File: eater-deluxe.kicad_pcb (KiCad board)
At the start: 2 copper layers, 214.2 x 149.5 mm, 39 parts, among them J1 PJ-202A, J2 DE9_Socket, SW1 RESET, U1 6502, U2 W65C22NxP, U3 W65C51NxP, U4 28C256, U5 HM62256BLP, U6 CD74HC00E, U7 MAX232, U8 LCD Module Connector, X1 MXO45-3C-1M000000, Y1 1.8432MHz

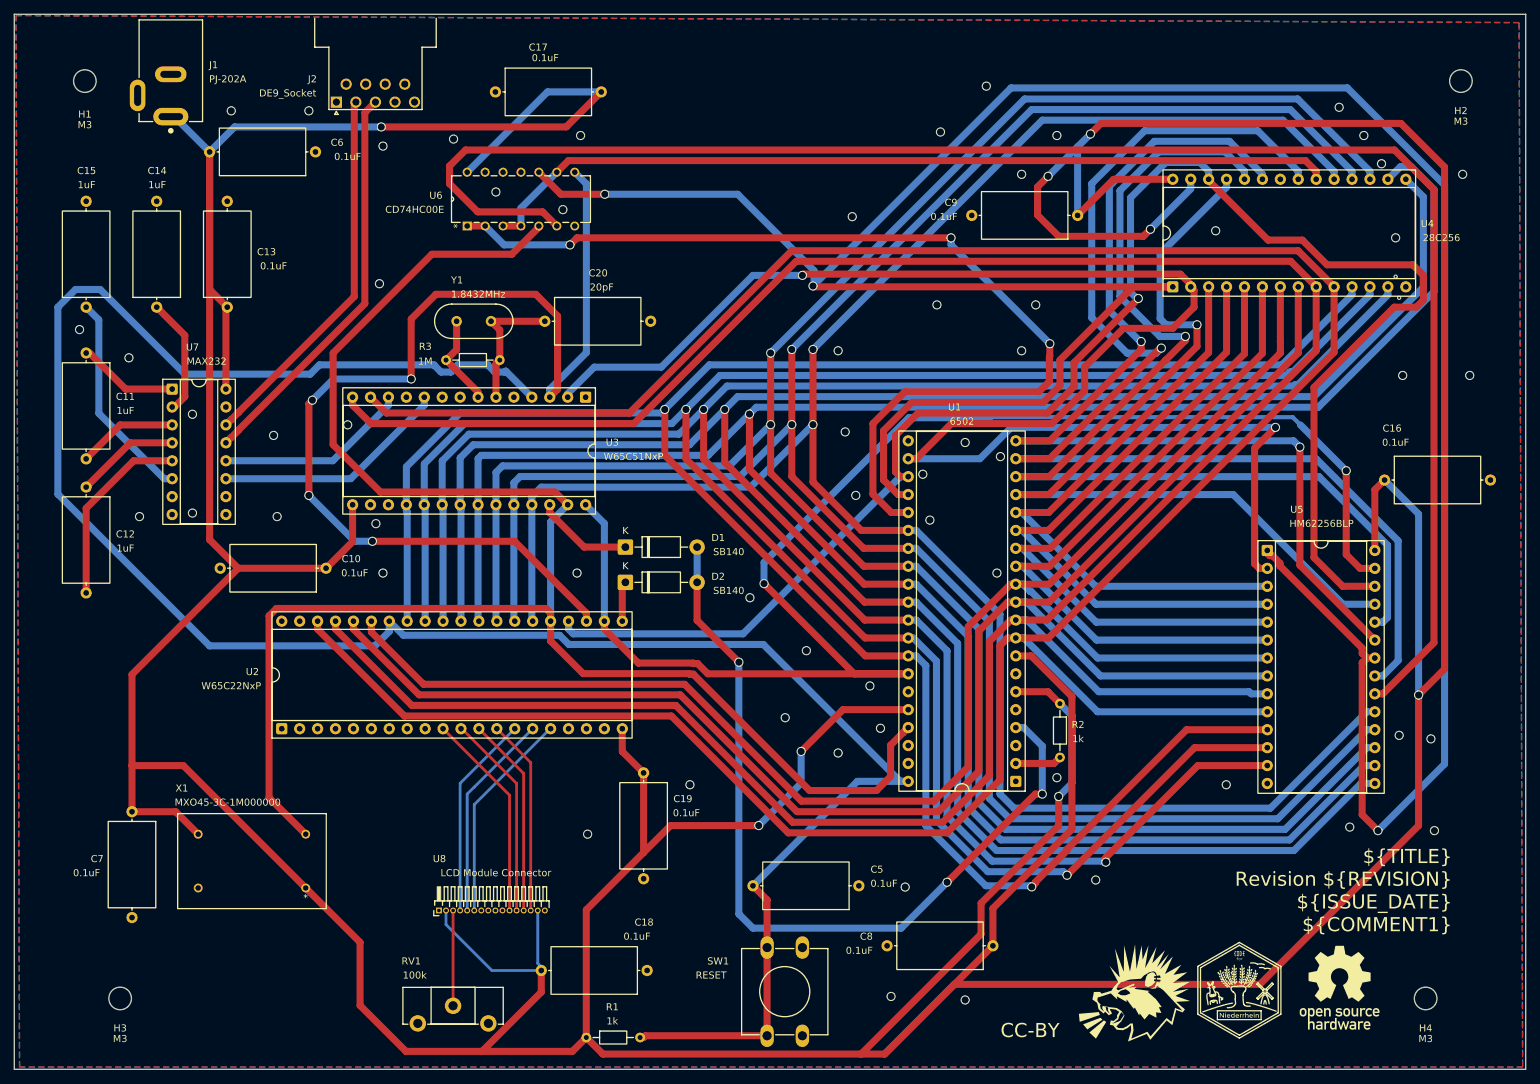
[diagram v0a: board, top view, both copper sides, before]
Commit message: Correct X1 pinout, fix LCD Pins, add pullup resistors for interrupt lines
Signed-off-by: Lucy Mielke <user@domain.tld>
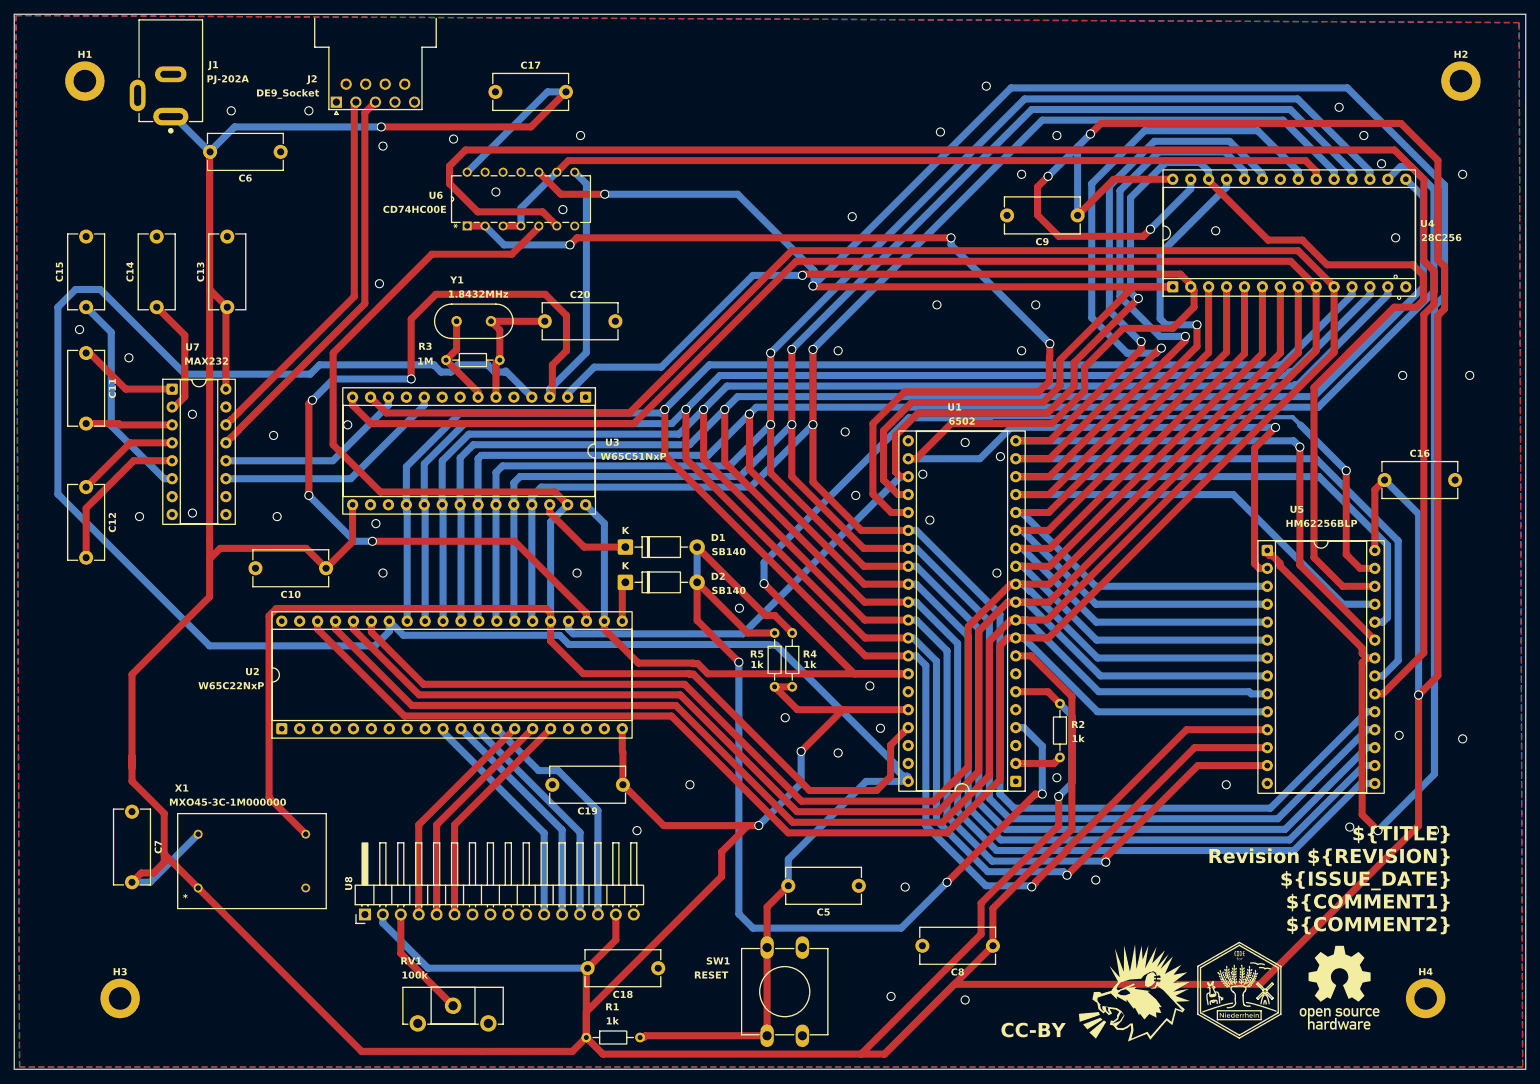
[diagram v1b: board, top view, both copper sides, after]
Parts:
- added R4: 1k, Resistor_THT:R_Axial_DIN0204_L3.6mm_D1.6mm_P7.62mm_Horizontal, F.Cu at (220.0, 156.5)
- added R5: 1k, Resistor_THT:R_Axial_DIN0204_L3.6mm_D1.6mm_P7.62mm_Horizontal, F.Cu at (217.5, 156.5)
- C10, C11, C12, C13, C14, C15, C16, C17, C18, C19, C20, C5, C6, C7, C8, C9: footprint Capacitor_THT:C_Axial_L12.0mm_D6.5mm_P15.00mm_Horizontal -> Capacitor_THT:C_Disc_D10.5mm_W5.0mm_P10.00mm
- H1, H2, H3, H4: value M3 -> MountingHole; footprint MountingHole:MountingHole_3.2mm_M3 -> MountingHole:MountingHole_3.2mm_M3_DIN965_Pad
- U8: footprint Connector_PinHeader_1.00mm:PinHeader_1x16_P1.00mm_Horizontal -> Connector_PinHeader_2.54mm:PinHeader_1x16_P2.54mm_Horizontal
- moved U8 10.5 mm to (159.4, 196.4)
- moved C6 4.93 mm to (147.5, 88.3)
- moved C19 3.38 mm to (196.0, 178.0), turned to 180 degrees
- moved C18 1.60 mm to (201.0, 204.0)
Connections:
- C7 pad 1: /5V -> GND
- C7 pad 2: GND -> /5V
- X1 pad 1: /5V -> GND
- X1 pad 4: GND -> /5V
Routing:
- net /IRQ: track 117.8 -> 150.3 mm
- net /5V: track 1018.4 -> 1041.9 mm
- net /PB3: track 27.7 -> 33.9 mm
- net Net-(U7-C2-): track 27.0 -> 22.0 mm
- net /PB2: track 28.4 -> 32.3 mm
- net /PB1: track 29.1 -> 32.4 mm
- net /PB4: track 29.0 -> 32.0 mm
- net /PB0: track 29.7 -> 32.3 mm
- net Net-(U8-V0): track 13.5 -> 16.0 mm
- net /PB5: track 29.6 -> 32.0 mm
- net Net-(U7-C1-): track 14.2 -> 12.3 mm
- net /CS2: track 155.0 -> 156.8 mm
- net /PB6: track 30.3 -> 32.0 mm
- net /RESET: track 312.5 -> 310.8 mm
- net GND: vias 63 -> 62
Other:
- board text added: "${TITLE} Revision ${REVISION} ${ISSUE_DATE} ${COMMENT1} ${COMMENT2}"
- board text removed: "${TITLE} Revision ${REVISION} ${ISSUE_DATE} ${COMMENT1}"
